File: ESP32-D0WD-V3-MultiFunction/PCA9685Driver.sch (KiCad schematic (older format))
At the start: 32 parts

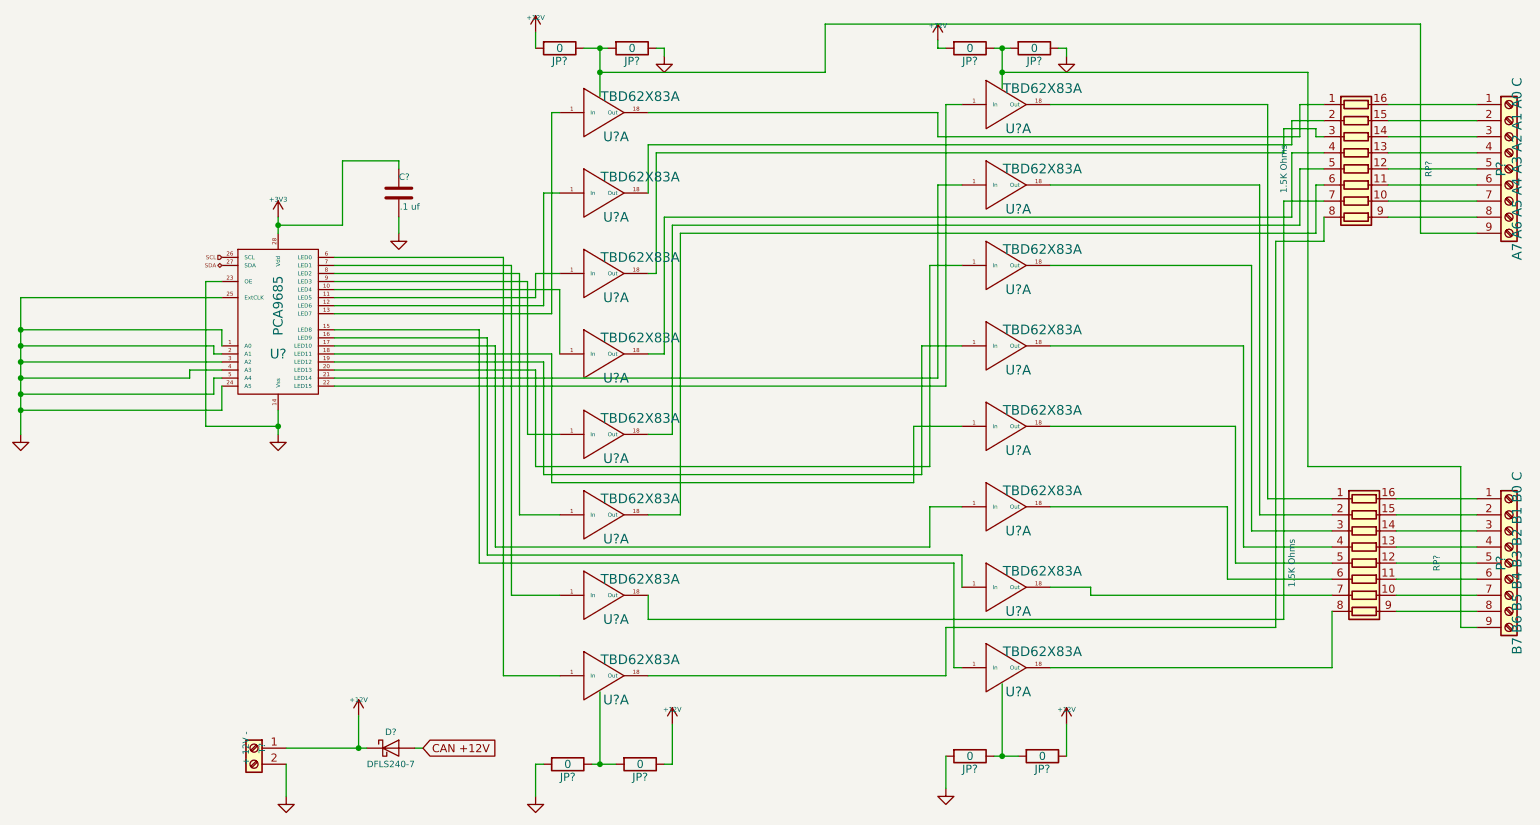
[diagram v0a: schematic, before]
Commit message: All but the MPU on the ESP32-D0WD-V3-MultiFunction is done.
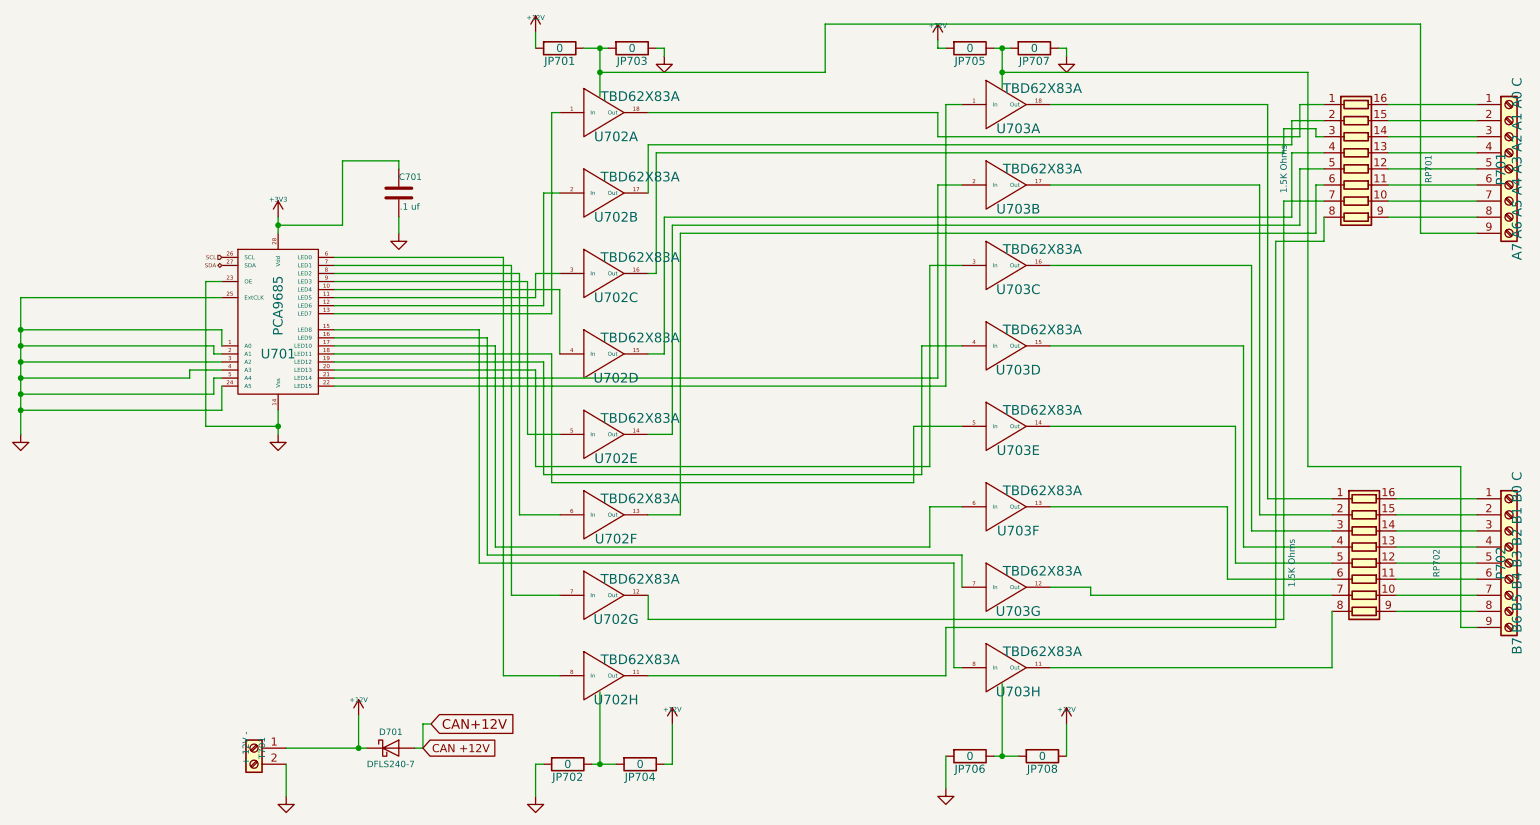
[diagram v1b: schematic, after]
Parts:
- gave numbers to parts that had none: 18
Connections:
- net at U701.10 (LED4): now also U702.4 (In); no longer U702.1 (In)
- net at U701.11 (LED5): now also U702.3 (In); no longer U702.1 (In)
- net at U701.12 (LED6): now also U702.2 (In); no longer U702.1 (In)
- net at U701.15 (LED8): now also U703.8 (In); no longer U703.1 (In)
- net at U701.16 (LED9): now also U703.7 (In); no longer U703.1 (In)
- net at U701.17 (LED10): now also U703.6 (In); no longer U703.1 (In)
- net at U701.18 (LED11): now also U703.5 (In); no longer U703.1 (In)
- net at U701.19 (LED12): now also U703.4 (In); no longer U703.1 (In)
- net at U701.20 (LED13): now also U703.3 (In); no longer U703.1 (In)
- net at U701.21 (LED14): now also U703.2 (In); no longer U703.1 (In)
- net at U701.6 (LED0): now also U702.8 (In); no longer U702.1 (In)
- net at U701.7 (LED1): now also U702.7 (In); no longer U702.1 (In)
- net at U701.8 (LED2): now also U702.6 (In); no longer U702.1 (In)
- net at U701.9 (LED3): now also U702.5 (In); no longer U702.1 (In)
- net at RP701.2 (R2.1): now also U702.17 (Out); no longer U702.18 (Out)
- net at RP701.3 (R3.1): now also U702.16 (Out); no longer U702.18 (Out)
- net at RP701.4 (R4.1): now also U702.15 (Out); no longer U702.18 (Out)
- net at RP701.5 (R5.1): now also U702.14 (Out); no longer U702.18 (Out)
- net at RP701.6 (R6.1): now also U702.13 (Out); no longer U702.18 (Out)
- net at RP701.7 (R7.1): now also U702.12 (Out); no longer U702.18 (Out)
- net at RP701.8 (R8.1): now also U702.11 (Out); no longer U702.18 (Out)
- net at RP702.2 (R2.1): now also U703.17 (Out); no longer U703.18 (Out)
- net at RP702.3 (R3.1): now also U703.16 (Out); no longer U703.18 (Out)
- net at RP702.4 (R4.1): now also U703.15 (Out); no longer U703.18 (Out)
- net at RP702.5 (R5.1): now also U703.14 (Out); no longer U703.18 (Out)
- net at RP702.6 (R6.1): now also U703.13 (Out); no longer U703.18 (Out)
- net at RP702.7 (R7.1): now also U703.12 (Out); no longer U703.18 (Out)
- net at RP702.8 (R8.1): now also U703.11 (Out); no longer U703.18 (Out)
